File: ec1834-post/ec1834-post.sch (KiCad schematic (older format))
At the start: 17 parts, among them U0 BUS_EC1834_8Bit, U1 7432, U2 74HC04, U3 7430, U4 74HC374, U5 2732, U6 2732

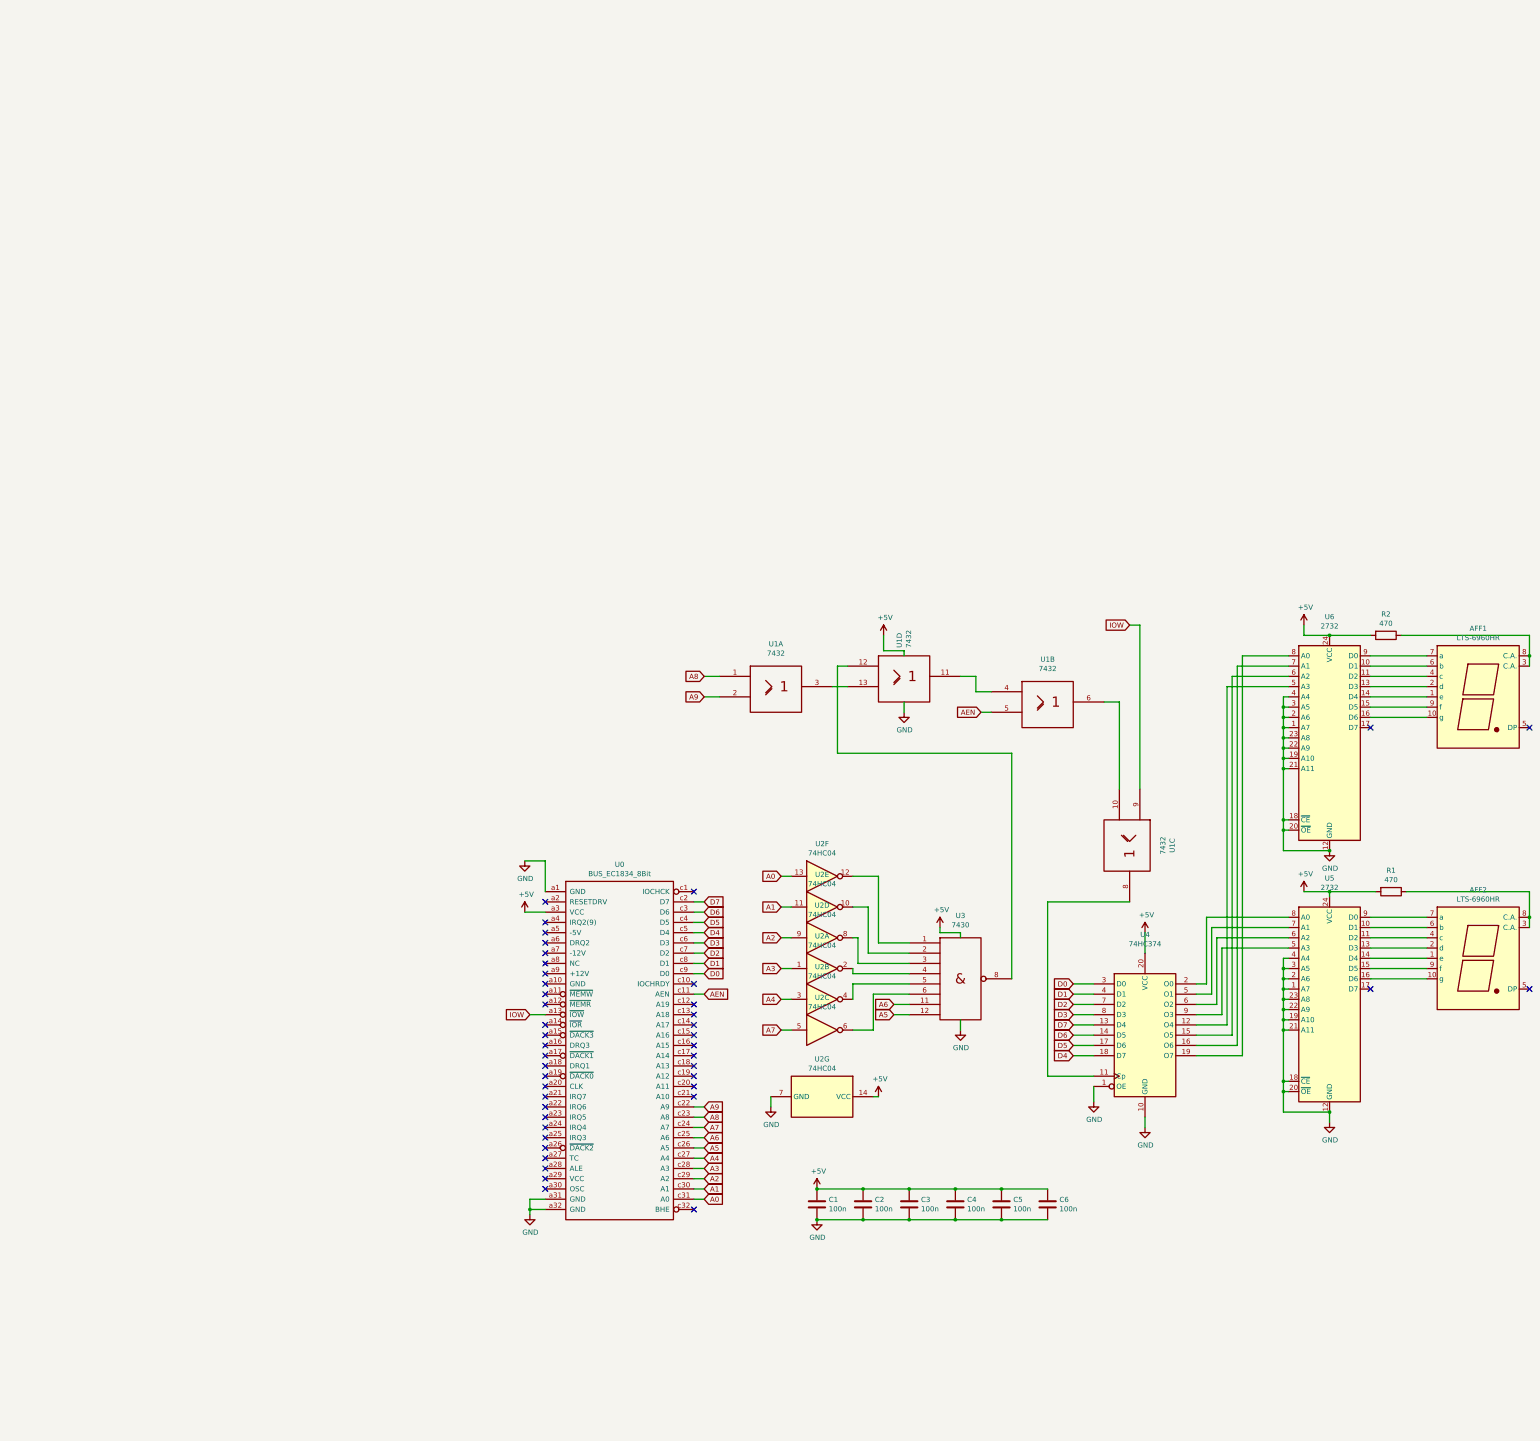
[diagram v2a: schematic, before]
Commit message: Added EPROM content Fixed DIP footprints (too wide) Added ISA BUS/Edge
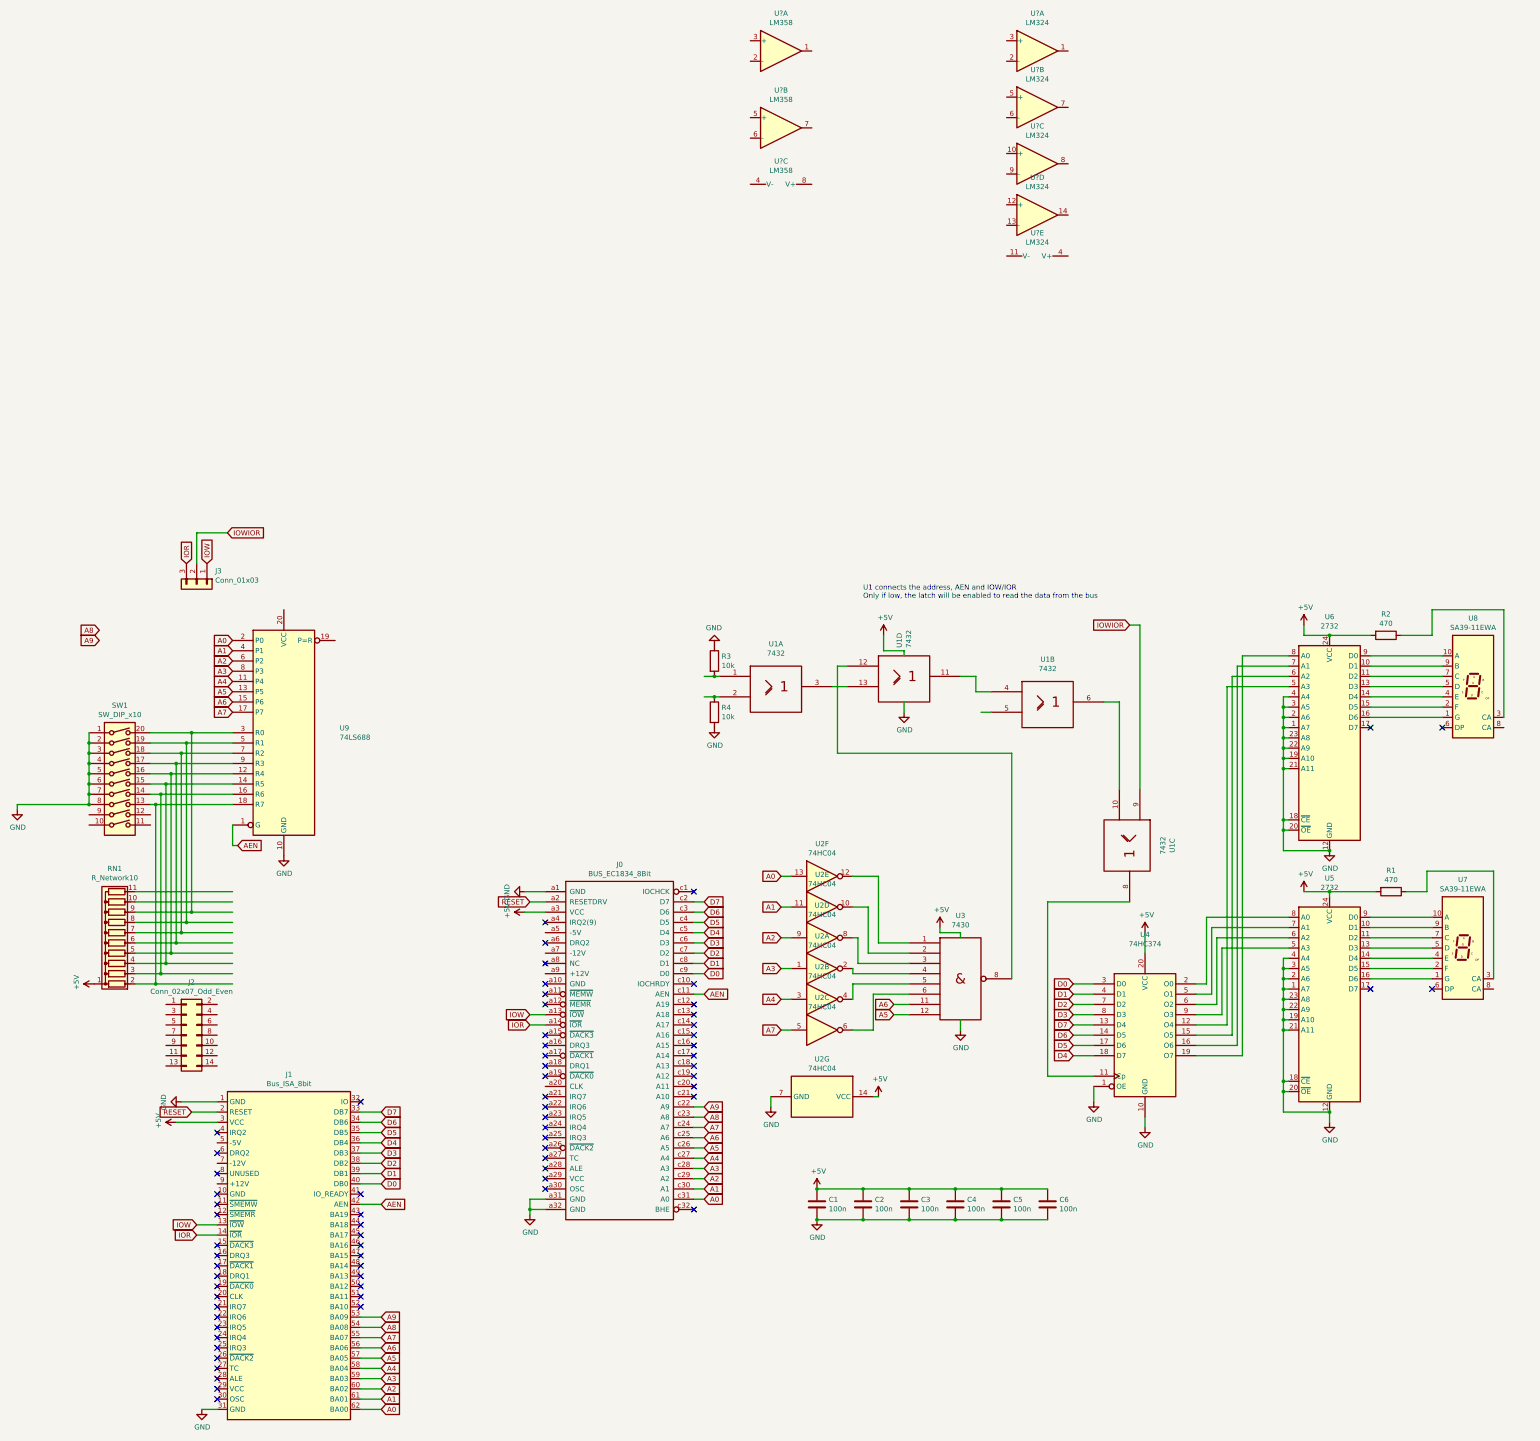
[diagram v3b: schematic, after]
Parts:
- removed AFF1, AFF2: LTS-6960HR, Display_7Segment:7SegmentLED_LTS6760_LTS6780, symbol Display_Character:LTS-6960HR
- added J1: Bus_ISA_8bit, Connector_PCBEdge:BUS_AT, symbol Connector:Bus_ISA_8bit
- added J2: Conn_02x07_Odd_Even, Connector_PinHeader_2.54mm:PinHeader_2x07_P2.54mm_Horizontal, symbol Connector_Generic:Conn_02x07_Odd_Even
- added J3: Conn_01x03, Connector_PinHeader_2.54mm:PinHeader_1x03_P2.54mm_Horizontal, symbol Connector_Generic:Conn_01x03
- added R3, R4: 10k, Resistor_THT:R_Axial_DIN0207_L6.3mm_D2.5mm_P7.62mm_Horizontal, symbol Device:R
- added RN1: R_Network10, Resistor_THT:R_Array_SIP11, symbol Device:R_Network10
- added SW1: SW_DIP_x10, Button_Switch_THT:SW_DIP_SPSTx10_Slide_9.78x27.58mm_W7.62mm_P2.54mm, symbol Switch:SW_DIP_x10
- added U7, U8: SA39-11EWA, Display_7Segment:Sx39-1xxxxx, symbol Display_Character:SA39-11EWA
- added U9: 74LS688, Package_DIP:DIP-20_W7.62mm, symbol 74xx:74LS688
- added U? (x3): LM358, symbol Amplifier_Operational:LM358
- added U? (x5): LM324, symbol Amplifier_Operational:LM324
- R1, R2: footprint Resistor_THT:R_Axial_DIN0309_L9.0mm_D3.2mm_P12.70mm_Horizontal -> Resistor_THT:R_Axial_DIN0207_L6.3mm_D2.5mm_P7.62mm_Horizontal
- U1: footprint Package_DIP:DIP-14_W10.16mm -> Package_DIP:DIP-16_W7.62mm
- U2, U3: footprint Package_DIP:DIP-14_W10.16mm -> Package_DIP:DIP-14_W7.62mm
- renumbered U0 to J0
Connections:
- net labels added: IOR, IOWIOR, RESET
- wire segments 193 -> 278
- no-connect marks 44 -> 72
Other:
- note added: "U1 connects the address, AEN and IOW/IOR\nOnly if low, the latch will be enabled to read the data from the bus"

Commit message: New revision routing still in progress
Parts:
- removed R4: 10k, Resistor_THT:R_Axial_DIN0207_L6.3mm_D2.5mm_P7.62mm_Horizontal, symbol Device:R
- removed U2: 74HC04, Package_DIP:DIP-14_W7.62mm, symbol 74xx:74HC04
- removed U3: 7430, Package_DIP:DIP-14_W7.62mm, symbol 74xx_IEEE:7430
- removed U? (x3): LM358, symbol Amplifier_Operational:LM358
- removed U? (x5): LM324, symbol Amplifier_Operational:LM324
- added C7: 100uF 6,3V, Capacitor_THT:CP_Radial_D6.3mm_P2.50mm, symbol Device:C
- added J4: Conn_02x06_Odd_Even, Connector_PinHeader_2.54mm:PinHeader_2x06_P2.54mm_Vertical, symbol Connector_Generic:Conn_02x06_Odd_Even
- added U2: 74LS86, Package_DIP:DIP-14_W7.62mm, symbol 74xx:74LS86
- C4: footprint Capacitor_THT:C_Axial_L5.1mm_D3.1mm_P7.50mm_Horizontal -> Capacitor_THT:C_Axial_L3.8mm_D2.6mm_P7.50mm_Horizontal
- C5, C6: footprint Capacitor_THT:C_Axial_L5.1mm_D3.1mm_P10.00mm_Horizontal -> Capacitor_THT:C_Axial_L3.8mm_D2.6mm_P7.50mm_Horizontal
- J1: footprint Connector_PCBEdge:BUS_AT -> Connector_PCBEdge:ISA-8BIT-XT-IDE
- J2: footprint Connector_PinHeader_2.54mm:PinHeader_2x07_P2.54mm_Horizontal -> Connector_PinHeader_2.54mm:PinHeader_2x07_P2.54mm_Vertical
- J3: footprint Connector_PinHeader_2.54mm:PinHeader_1x03_P2.54mm_Horizontal -> Connector_PinHeader_2.54mm:PinHeader_1x03_P2.54mm_Vertical
- R3: value 10k -> 2K2
- renumbered U9 to U1, U1 to U3
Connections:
- net labels added: +12V, -12V, -5V, CLK, DB0, DB1, DB2, DB3, DB4, DB5, DB6, DB7, ENLATCH, SELA8, SELA9, SEL_AD, SW_A8, SW_A9
- no-connect marks 72 -> 81
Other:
- moved on the sheet: C1, C2, C3, C4, C5, C6, J0, J2, J3, RN1, SW1, U1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

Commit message: Rebuild of PCB is done
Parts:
- added C8: 100n, Capacitor_THT:C_Axial_L3.8mm_D2.6mm_P7.50mm_Horizontal, symbol Device:C
- added U9: 74HC374, Package_DIP:DIP-20_W7.62mm, symbol 74xx:74HC374
- C7: value 100uF 6,3V -> 100uF
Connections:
- net labels added: J2D0, J2D1, J2D2, J2D3, J2D4, J2D5, J2D6, J2D7
- wire segments 278 -> 298
- no-connect marks 81 -> 78
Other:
- moved on the sheet: R3, U2A, U2B, U2C, U2D, U2E, U3A, U4

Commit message: Updated schema, fixed wrong footprint
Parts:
- U3: footprint Package_DIP:DIP-16_W7.62mm -> Package_DIP:DIP-14_W7.62mm
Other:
- moved on the sheet: C1, C2, C3, C4, C5, C6, C7, C8, J0, J1, J2, J3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
